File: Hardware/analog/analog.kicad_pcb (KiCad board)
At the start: 4 copper layers, 128 x 182 mm, 131 parts, among them J201 Würth 74651194R, J202 Würth 74651194R, J301 Conn_02x10_Odd_Even, J501 Conn_01x01, J502 Conn_01x01, M501 Fan_4pin, Q201 IXTH80N075L2, Q202 IXTH80N075L2, Q501 MMBT3904, U201 ADA4522-2, U202 LM431SC, U203 LMT86LMT, U204 ADA4522-2, U205 LM431SC, U206 LMT86LMT, U301 ADUM131D, U302 ADUM131D, U303 ADUM1250, U304 74LVC1G19, U305 AT24CS32-SSHM, U401 ICL7660, U402 MCP1804x-C002xMB, U403 MCP1703AT-5002E/DB, U404 XC6203E33, U405 LP5907MFX-3.3, U501 EMC2101-R, U601 MCP3562, U602 MAX6166, U603 DAC8562, U701 Si5351A-B-GT, Y701 25MHz

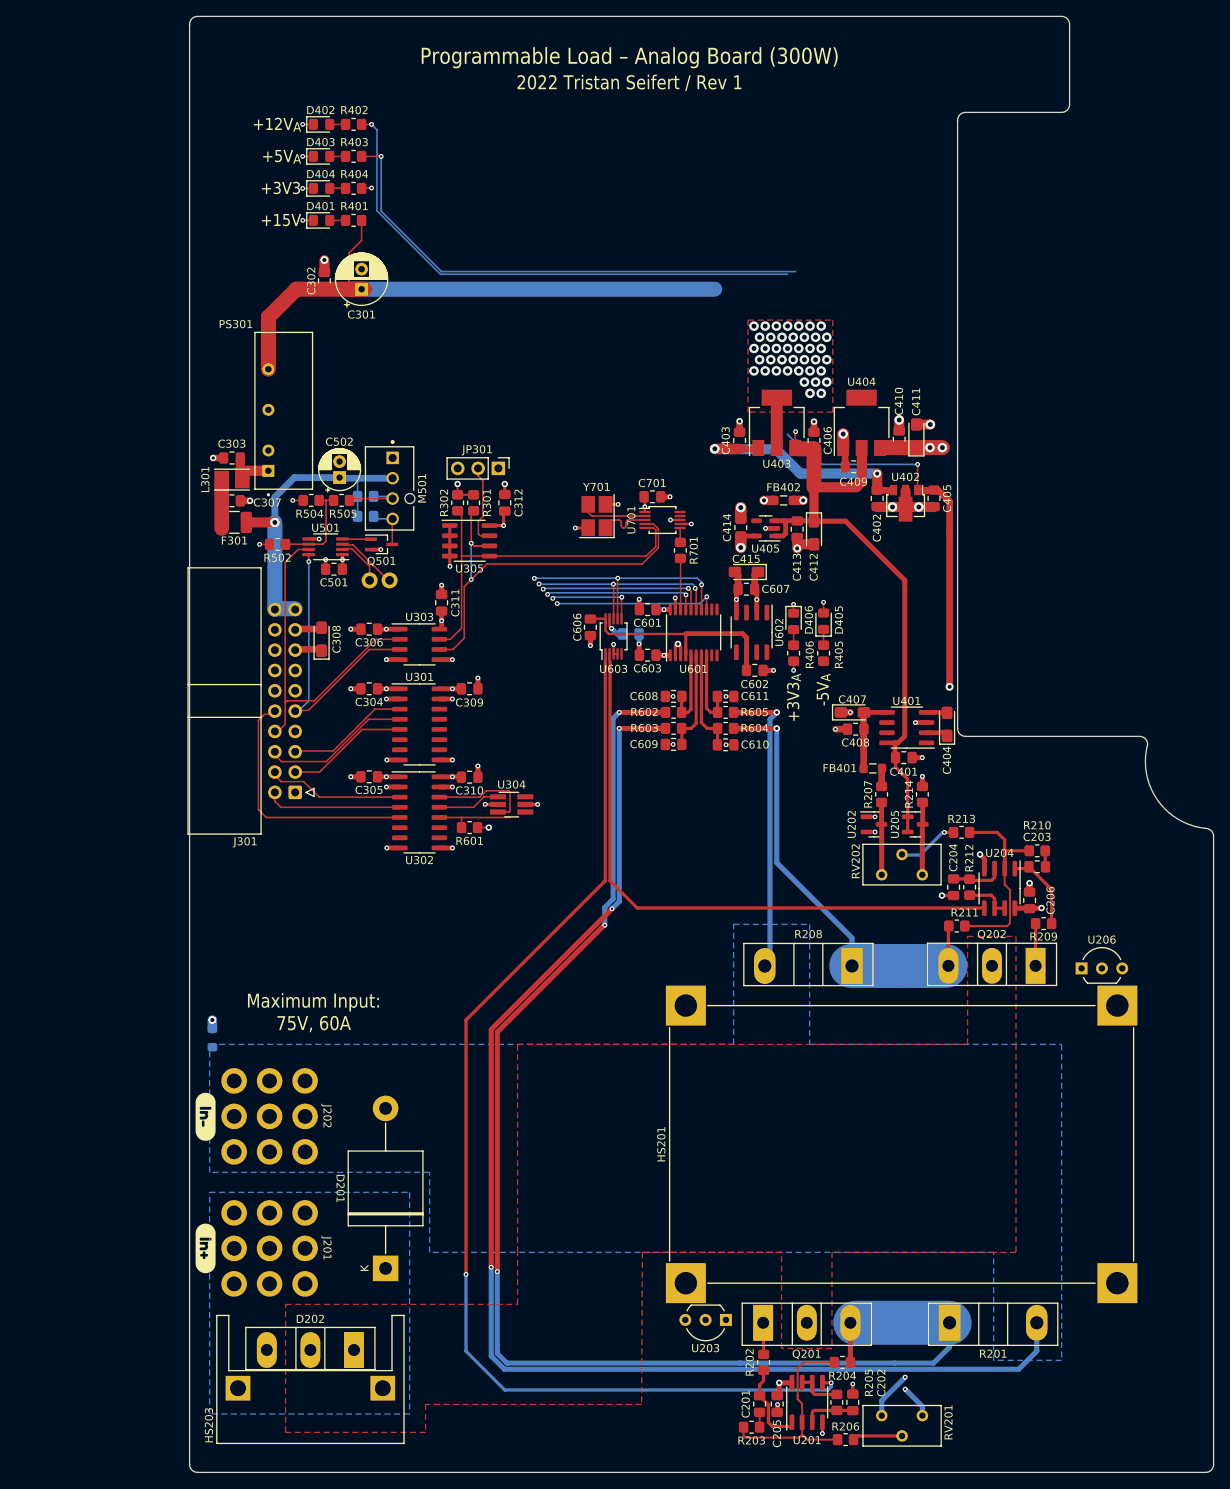
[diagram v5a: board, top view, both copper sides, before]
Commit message: Analog board layout
- Started work on adding the voltage sense circuitry, including the
  selector relay, IO expander to drive the relay, and the second ADC to
  convert the voltage values

- Changed the layout of analog board to better take advantage of
  available space

- Minor changes to front panel layout for aesthetics
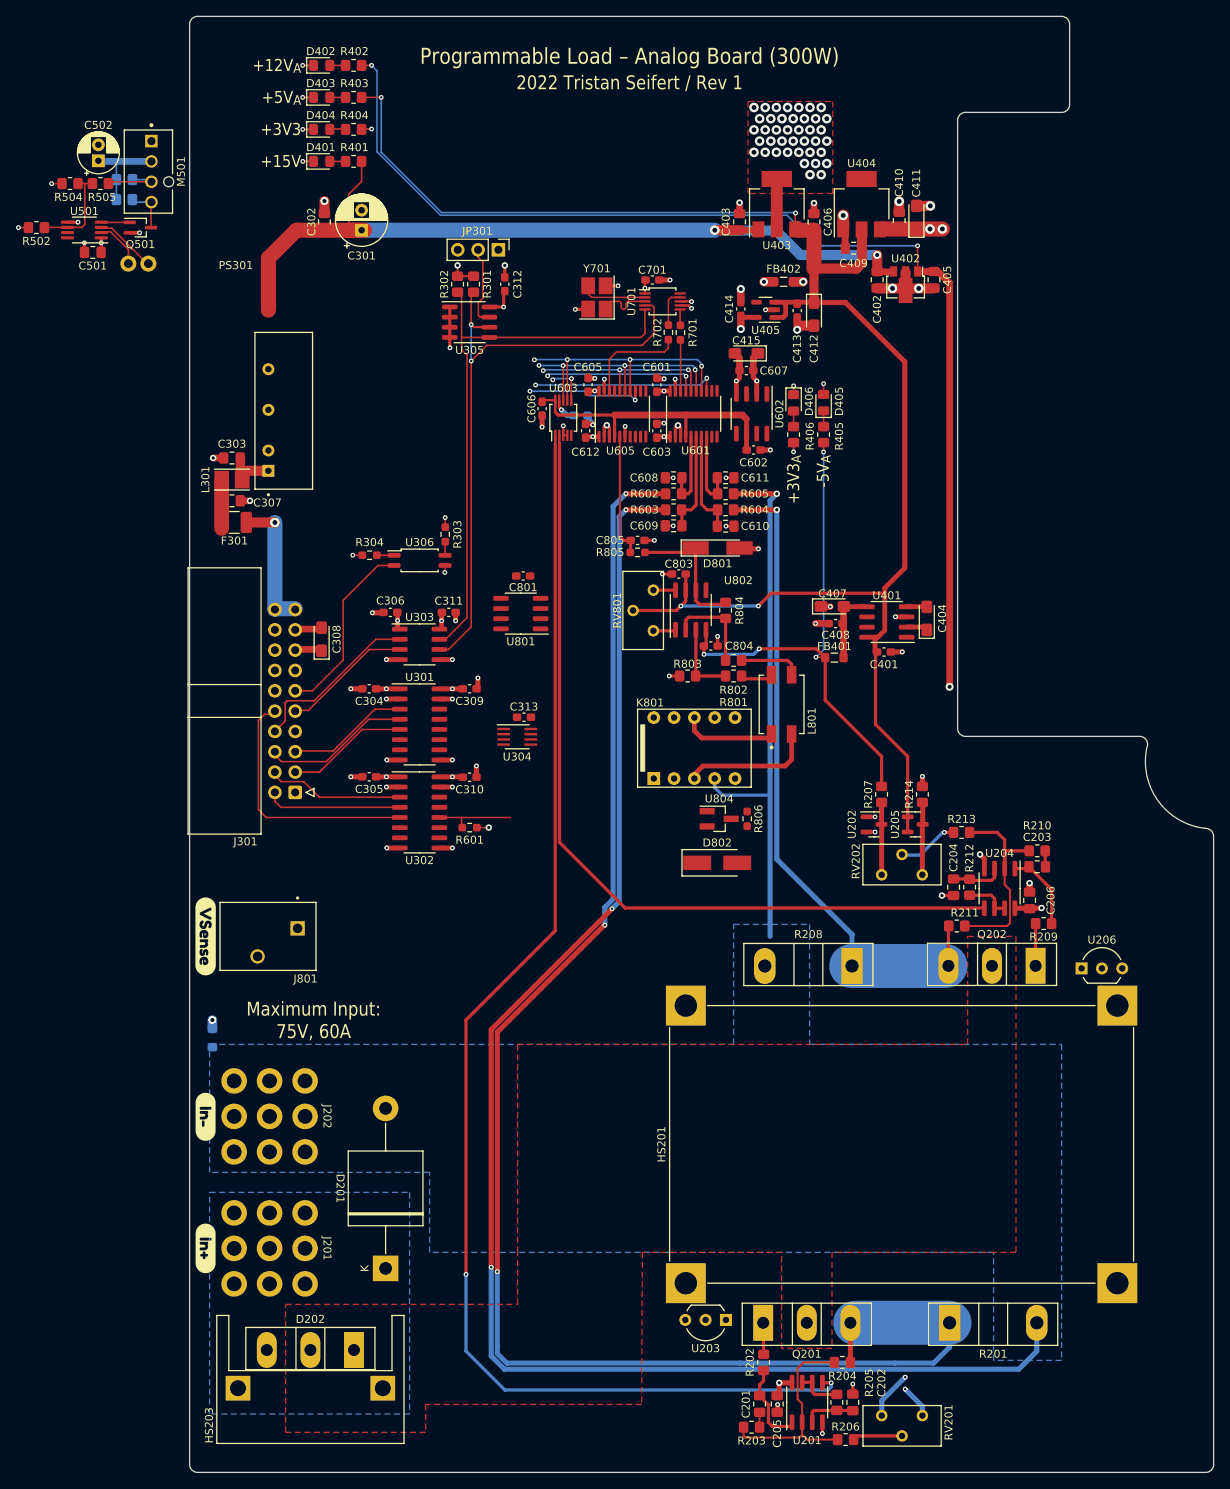
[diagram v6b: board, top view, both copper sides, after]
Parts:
- added C313: 100nF, Capacitor_SMD:C_0603_1608Metric_Pad1.08x0.95mm_HandSolder, F.Cu at (61.8, 107.6)
- added C605: 100nF, Capacitor_SMD:C_0603_1608Metric_Pad1.08x0.95mm_HandSolder, F.Cu at (69.8, 66.0)
- added C612: 100nF, Capacitor_SMD:C_0603_1608Metric_Pad1.08x0.95mm_HandSolder, F.Cu at (69.5, 71.8)
- added C801: 100nF, Capacitor_SMD:C_0603_1608Metric_Pad1.08x0.95mm_HandSolder, F.Cu at (61.7, 90.0)
- added C803: 100nF, Capacitor_SMD:C_0603_1608Metric_Pad1.08x0.95mm_HandSolder, F.Cu at (81.2, 89.7)
- added C804: 100nF, Capacitor_SMD:C_0603_1608Metric_Pad1.08x0.95mm_HandSolder, F.Cu at (85.2, 98.7)
- added C805: 100nF, Capacitor_SMD:C_0603_1608Metric_Pad1.08x0.95mm_HandSolder, F.Cu at (76.0, 85.5)
- added D801: 2V4, Diode_SMD:D_MiniMELF_Handsoldering, F.Cu at (86.0, 86.5)
- added D802: SM4007, Diode_SMD:D_SMA_Handsoldering, F.Cu at (86.0, 125.8)
- added J801: Conn_01x02, programmable-load:CUI_TBL002A-350-02GR-2OR, F.Cu at (33.5, 134.0)
- added K801: EA2-3T, programmable-load:KEMET-EA2, F.Cu at (76.0, 116.0)
- added L801: L_Ferrite_Coupled_1423, programmable-load:Bourns-DR331-0-0-MFG, F.Cu at (94.0, 106.0)
- added R303: 10k, Resistor_SMD:R_0603_1608Metric_Pad0.98x0.95mm_HandSolder, F.Cu at (52.0, 84.8)
- added R304: 200R, Resistor_SMD:R_0603_1608Metric_Pad0.98x0.95mm_HandSolder, F.Cu at (42.5, 87.3)
- added R702: 0R, Resistor_SMD:R_0603_1608Metric_Pad0.98x0.95mm_HandSolder, F.Cu at (79.8, 59.5)
- added R801: 1M .1%, Resistor_SMD:R_0805_2012Metric_Pad1.20x1.40mm_HandSolder, F.Cu at (88.0, 102.5)
- added R802: 1M .1%, Resistor_SMD:R_0805_2012Metric_Pad1.20x1.40mm_HandSolder, F.Cu at (88.0, 100.5)
- added R803: 20k .1%, Resistor_SMD:R_0805_2012Metric_Pad1.20x1.40mm_HandSolder, F.Cu at (82.2, 102.5)
- added R804: 20k .1%, Resistor_SMD:R_0805_2012Metric_Pad1.20x1.40mm_HandSolder, F.Cu at (87.0, 94.2)
- added R805: 4k99, Resistor_SMD:R_0603_1608Metric_Pad0.98x0.95mm_HandSolder, F.Cu at (76.0, 87.0)
- added R806: 4k7, Resistor_SMD:R_0603_1608Metric_Pad0.98x0.95mm_HandSolder, F.Cu at (89.7, 120.3)
- added RV801: 20k, programmable-load:Potentiometer_Nidec_Copal_CT94EY, F.Cu at (78.0, 96.8)
- added U306: FODM217B, Package_SO:SOP-4_4.4x2.6mm_P1.27mm, F.Cu at (48.8, 88.0)
- added U605: MCP3561, Package_SO:TSSOP-20_4.4x6.5mm_P0.65mm, F.Cu at (74.1, 69.7)
- added U801: PCA9536D, Package_SO:SOIC-8_3.9x4.9mm_P1.27mm, F.Cu at (61.4, 94.7)
- added U802: OPA277, Package_SO:SOIC-8_3.9x4.9mm_P1.27mm, F.Cu at (82.7, 94.2)
- added U804: MMBT3904, Package_TO_SOT_SMD:SOT-23_Handsoldering, F.Cu at (86.2, 120.3)
- added kibuzzard-6291C153: G***, kibuzzard-6291C153, F.Cu at (22.0, 135.0)
- C304, C305, C306, C309, C310, C311, C312, C401, C408, C413, C414, C601, C602, C603, C604, C606, C607, C701: footprint Capacitor_SMD:C_0805_2012Metric_Pad1.18x1.45mm_HandSolder -> Capacitor_SMD:C_0603_1608Metric_Pad1.08x0.95mm_HandSolder
- R601, R701: footprint Resistor_SMD:R_0805_2012Metric_Pad1.20x1.40mm_HandSolder -> Resistor_SMD:R_0603_1608Metric_Pad0.98x0.95mm_HandSolder
- U304: value 74LVC1G19 -> 74LVC1G139; footprint Package_TO_SOT_SMD:TSOT-23-6_HandSoldering -> Package_SO:SSOP-8_2.95x2.8mm_P0.65mm
- moved C501 49.8 mm to (7.90, 49.5)
- moved C502 49.8 mm to (8.60, 38.0)
- moved J501 49.8 mm to (12.3, 50.9)
- moved J502 49.8 mm to (14.8, 50.9)
- moved M501 49.8 mm to (14.8, 39.4)
- moved Q501 49.8 mm to (13.8, 46.4)
- moved R502 49.8 mm to (0.85, 46.4)
- moved R503 49.8 mm to (11.8, 42.9)
- moved R504 49.8 mm to (5.05, 40.9)
- moved R505 49.8 mm to (8.85, 40.9)
- moved R506 49.8 mm to (11.8, 40.4)
- moved U501 49.8 mm to (6.85, 46.7)
- moved C601 28.1 mm to (78.4, 66.0), turned to 90 degrees
- moved C603 28.1 mm to (78.4, 71.8), turned to 90 degrees
- moved C604 28.0 mm to (68.9, 69.9)
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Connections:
- net /Analog stuff/ADCCLK renamed /Analog stuff/ADCCLK_{0}
- net /Analog stuff/Sense_{0+ renamed /Analog stuff/Sense_{0+}
- net /Analog stuff/Sense_{0- renamed /Analog stuff/Sense_{0-}
- net /Analog stuff/Sense_{1+ renamed /Analog stuff/Sense_{1+}
- net /Analog stuff/Sense_{1- renamed /Analog stuff/Sense_{1-}
- Q201 pad 3: /MOSFET Load/ISense_{0} -> /ISense_{0}
- Q202 pad 3: /MOSFET Load/ISense_{1} -> /ISense_{1}
- R201 pad 1: /MOSFET Load/ISense_{0} -> /ISense_{0}
- R204 pad 2: /MOSFET Load/ISense_{0} -> /ISense_{0}
- R208 pad 1: /MOSFET Load/ISense_{1} -> /ISense_{1}
- R211 pad 2: /MOSFET Load/ISense_{1} -> /ISense_{1}
- U304 pad 1: /External Interface/SEL_0 -> unconnected-(U304-A)
- U304 pad 2: GND -> unconnected-(U304-B)
- U304 pad 3: /External Interface/~{SEL_EN} -> unconnected-(U304-Y3)
- U304 pad 4: /Analog stuff/~{CS_ADC} -> GND
- U304 pad 5: +3V3 -> unconnected-(U304-Y2)
- U304 pad 6: /Analog stuff/~{CS_DAC} -> unconnected-(U304-Y1)
- U601 pad 13: /Analog stuff/~{CS_ADC} -> /Analog stuff/~{CS_ADC_{0}}
- U603 pad 5: unconnected-(U603-~{CLR}) -> /External Interface/~{RESET}
- U701 pad 9: unconnected-(U701-CLK1) -> Net-(U701-CLK1)
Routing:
- net /ISense_{0}: track 0.00 -> 196.6 mm, vias 0 -> 3
- net /MOSFET Load/ISense_{0}: track 169.8 -> 0.00 mm, vias 3 -> 0
- net /ISense_{1}: track 0.00 -> 83.1 mm, vias 0 -> 1
- net +5VA: track 143.3 -> 209.3 mm, vias 2 -> 4
- net -5VA: track 2.40 -> 66.5 mm, vias 0 -> 4
- net GNDPWR: track 202.0 -> 261.5 mm
- net /MOSFET Load/ISense_{1}: track 55.8 -> 0.00 mm, vias 1 -> 0
- net /ISet_{1}: track 76.6 -> 107.3 mm
- net +12VA: track 255.9 -> 283.2 mm
- net /I2C_SCL: track 53.8 -> 80.3 mm
- net /I2C_SDA: track 46.3 -> 71.7 mm
- net /ISet_{0}: track 143.8 -> 168.4 mm
- net /Analog stuff/~{CS_ADC_{0}}: track 0.00 -> 23.3 mm, vias 0 -> 2
- net /External Interface/~{IN_RESET}: track 0.00 -> 23.2 mm
- net IN_I2C_SDA: track 43.3 -> 21.7 mm
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
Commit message: Mostly finished up analog load board
- Finished routing most signals

- Connected relay drive to bonus I2C GPIO controller, and routed the
  rest of the voltage sense stuff

- Routed the reset signal to the DAC, so that when the board is reset,
  the current output will be reset to zero as well without processor
  intervention

- Replaced most passives with 0603/1608 size
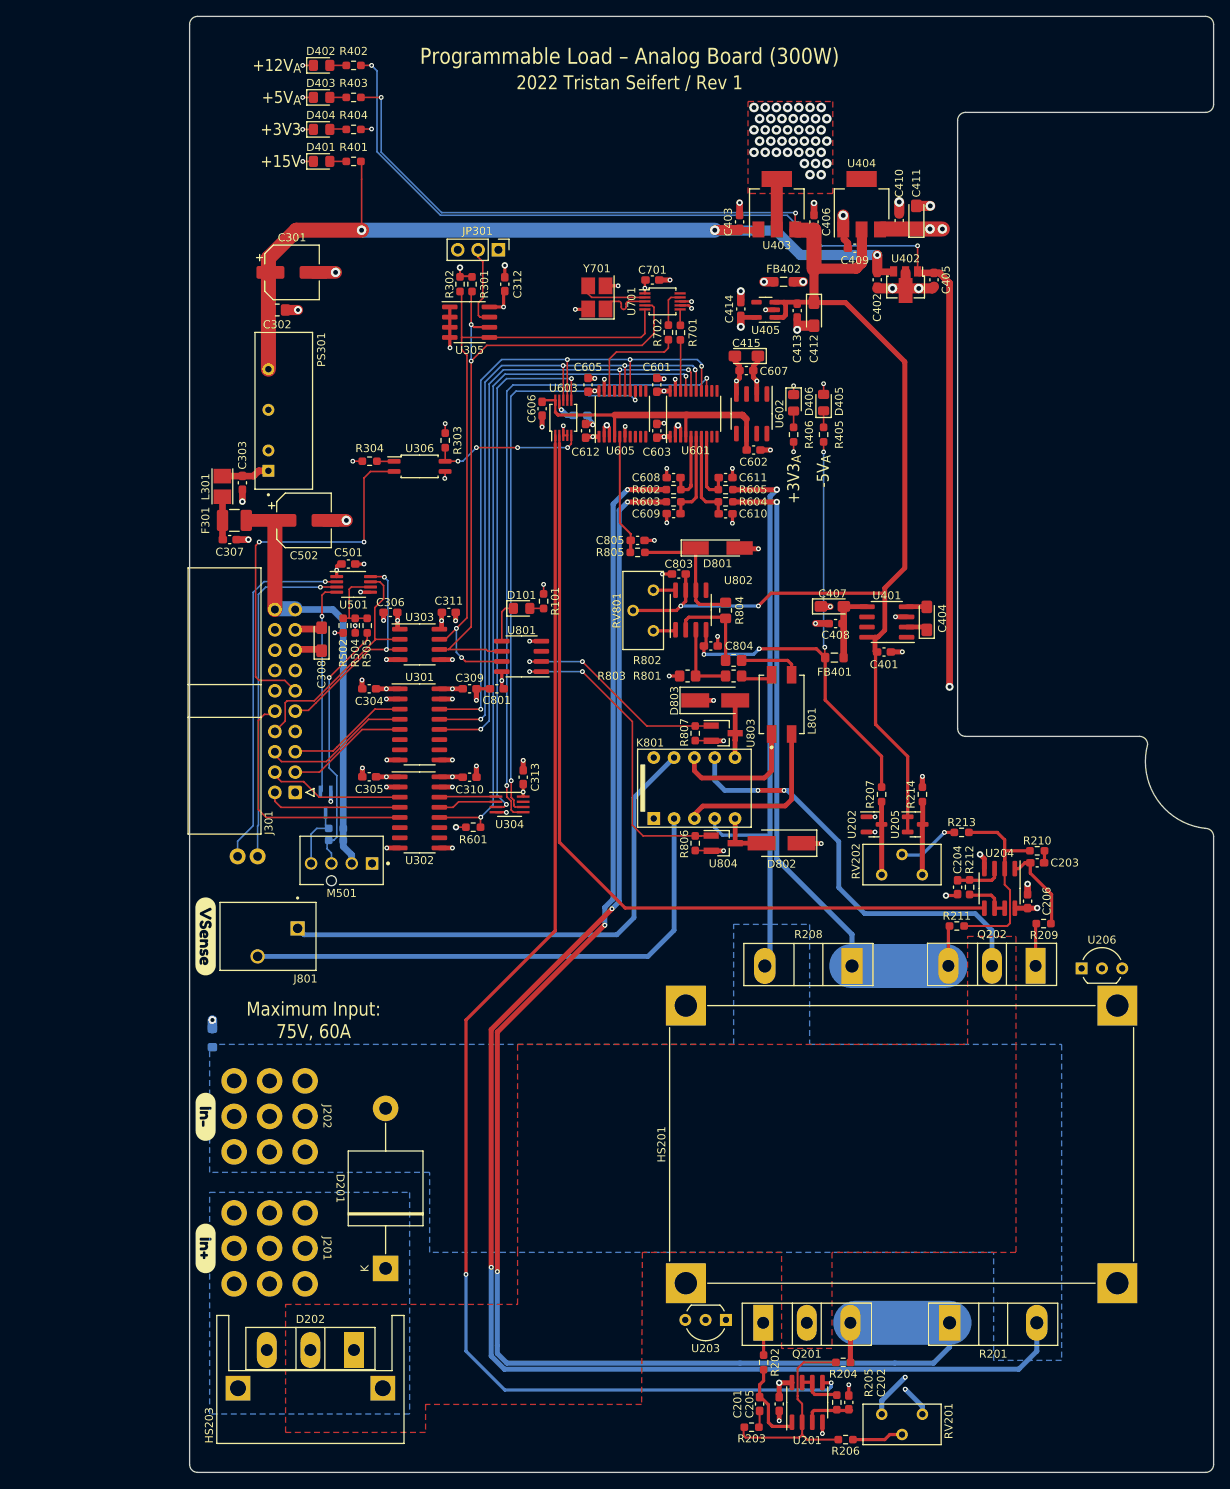
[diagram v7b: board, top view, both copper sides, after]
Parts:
- added D101: Red, LED_SMD:LED_0805_2012Metric_Pad1.15x1.40mm_HandSolder, F.Cu at (61.5, 94.0)
- added D803: SM4007, Diode_SMD:D_SMA_Handsoldering, F.Cu at (85.7, 105.5)
- added R101: 1k, Resistor_SMD:R_0603_1608Metric_Pad0.98x0.95mm_HandSolder, F.Cu at (64.2, 93.1)
- added R807: 4k7, Resistor_SMD:R_0603_1608Metric_Pad0.98x0.95mm_HandSolder, F.Cu at (83.2, 109.6)
- added U803: MMBT3904, Package_TO_SOT_SMD:SOT-23_Handsoldering, F.Cu at (86.7, 109.6)
- C201, C202, C203, C204, C205, C206, C303, C307, C402, C403, C405, C406, C409, C410, C501, C608, C609, C610, C611: footprint Capacitor_SMD:C_0805_2012Metric_Pad1.18x1.45mm_HandSolder -> Capacitor_SMD:C_0603_1608Metric_Pad1.08x0.95mm_HandSolder
- C301: value 47µF -> 33µF; footprint Capacitor_THT:CP_Radial_D6.3mm_P2.50mm -> Capacitor_SMD:CP_Elec_6.3x5.7
- C502: value 10µF -> 33µF; footprint Capacitor_THT:CP_Radial_D5.0mm_P2.00mm -> Capacitor_SMD:CP_Elec_6.3x5.7
- Q501: moved to B.Cu
- R202, R203, R204, R205, R206, R207, R209, R210, R211, R212, R213, R214, R301, R302, R401, R402, R403, R404, R405, R406, R502, R503, R504, R505, R506, R602, R603, R604, R605: footprint Resistor_SMD:R_0805_2012Metric_Pad1.20x1.40mm_HandSolder -> Resistor_SMD:R_0603_1608Metric_Pad0.98x0.95mm_HandSolder
- moved M501 89.4 mm to (39.0, 125.5), turned to 0 degrees
- moved R506 86.7 mm to (38.3, 123.0), turned to 0 degrees
- moved R503 82.9 mm to (38.3, 121.5), turned to 0 degrees
- moved Q501 75.5 mm to (37.0, 118.2), turned to -90 degrees
- moved J501 75.3 mm to (26.0, 125.0)
- moved J502 75.3 mm to (28.5, 125.0)
- moved R504 65.8 mm to (40.7, 96.2), turned to 90 degrees
- moved R505 64.5 mm to (42.2, 96.2), turned to 90 degrees
- moved R502 62.8 mm to (39.2, 96.2), turned to 90 degrees
- moved U501 55.6 mm to (40.5, 91.0), turned to 0 degrees
- moved C502 51.8 mm to (34.3, 83.0), turned to 0 degrees
- moved C501 50.4 mm to (39.9, 88.5), turned to 0 degrees
- moved C801 14.5 mm to (58.4, 104.0)
- moved C302 12.5 mm to (30.9, 56.7), turned to 0 degrees
- moved R303 11.8 mm to (52.0, 73.0)
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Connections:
- D802 pad 1: +12V -> +3V3
- D802 pad 2: Net-(U804-C) -> /Voltage Sense/RELAY_SET
- J301 pad 1: /External Interface/IN_SPI_SSEL1 -> /External Interface/IN_SPI_SSEL2
- J301 pad 2: /External Interface/IN_SPI_SSEL0 -> /External Interface/IN_SPI_SSEL1
- J301 pad 4: /External Interface/~{IN_SPI_CS} -> /External Interface/IN_SPI_SSEL0
- J801 pad 1: unconnected-(J801-Pin_1) -> /Voltage Sense/EXT_SENSE+
- J801 pad 2: unconnected-(J801-Pin_2) -> /Voltage Sense/EXT_SENSE-
- K801 pad 2: unconnected-(K801-Pad2) -> /Voltage Sense/EXT_SENSE-
- K801 pad 5: unconnected-(K801-Pad5) -> /Voltage Sense/RELAY_SET
- K801 pad 6: unconnected-(K801-Pad6) -> /Voltage Sense/RELAY_RESET
- K801 pad 9: unconnected-(K801-Pad9) -> /Voltage Sense/EXT_SENSE+
- R806 pad 2: /Voltage Sense/SW -> /Voltage Sense/IO_RLY_SET
- U302 pad 13: /External Interface/SEL_0 -> /External Interface/SEL_1
- U302 pad 14: /External Interface/~{SEL_EN} -> /External Interface/SEL_0
- U302 pad 3: /External Interface/~{IN_SPI_CS} -> /External Interface/IN_SPI_SSEL0
- U302 pad 4: /External Interface/IN_SPI_SSEL0 -> /External Interface/IN_SPI_SSEL1
- U304 pad 1: unconnected-(U304-A) -> /External Interface/SEL_0
- U304 pad 2: unconnected-(U304-B) -> /External Interface/SEL_1
- U304 pad 3: unconnected-(U304-Y3) -> /Analog stuff/~{CS_DAC}
- U304 pad 5: unconnected-(U304-Y2) -> /Analog stuff/~{CS_ADC_{0}}
- U304 pad 6: unconnected-(U304-Y1) -> /Analog stuff/~{CS_ADC_{1}}
- U304 pad 8: VCC -> +3V3
- U801 pad 1: unconnected-(U801-IO0) -> /Voltage Sense/IO_RLY_SET
- U801 pad 2: unconnected-(U801-IO1) -> /Voltage Sense/IO_RLY_RESET
- U801 pad 5: unconnected-(U801-IO3) -> /LED_STATUS
- U804 pad 1: /Voltage Sense/SW -> /Voltage Sense/IO_RLY_SET
- U804 pad 3: Net-(U804-C) -> /Voltage Sense/RELAY_SET
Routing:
- net /Voltage Sense/EXT_SENSE-: track 0.00 -> 67.4 mm
- net /Voltage Sense/EXT_SENSE+: track 0.00 -> 65.4 mm
- net /Analog stuff/~{CS_DAC}: track 5.07 -> 66.4 mm
- net /Analog stuff/~{IRQ}: track 29.5 -> 87.7 mm
- net /Analog stuff/~{CS_ADC_{0}}: track 23.3 -> 81.5 mm
- net /Analog stuff/SPI_MISO: track 23.6 -> 79.8 mm
- net /Analog stuff/~{CS_ADC_{1}}: track 14.8 -> 70.0 mm
- net /Analog stuff/SPI_MOSI: track 30.1 -> 85.2 mm
- net /Analog stuff/SPI_SCK: track 33.5 -> 87.6 mm
- net +VDC: track 0.00 -> 53.1 mm, vias 0 -> 2
- net /Voltage Sense/IO_RLY_SET: track 0.00 -> 41.0 mm, vias 0 -> 2
- net /Fan Control & Temperature Sensors/TEMP_DP: track 6.10 -> 44.8 mm, vias 0 -> 1
- net /Fan Control & Temperature Sensors/TEMP_DN: track 7.76 -> 43.0 mm, vias 0 -> 1
- net /Voltage Sense/IO_RLY_RESET: track 0.00 -> 27.5 mm, vias 0 -> 2
- net VBUS: track 29.0 -> 54.2 mm, vias 1 -> 0
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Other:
- outline, holes or cut-outs redrawn
